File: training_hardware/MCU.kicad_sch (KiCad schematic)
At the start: 2 parts, among them J1 RJ45_LED_Shielded, U1 Teensy4.1_DEV-16771

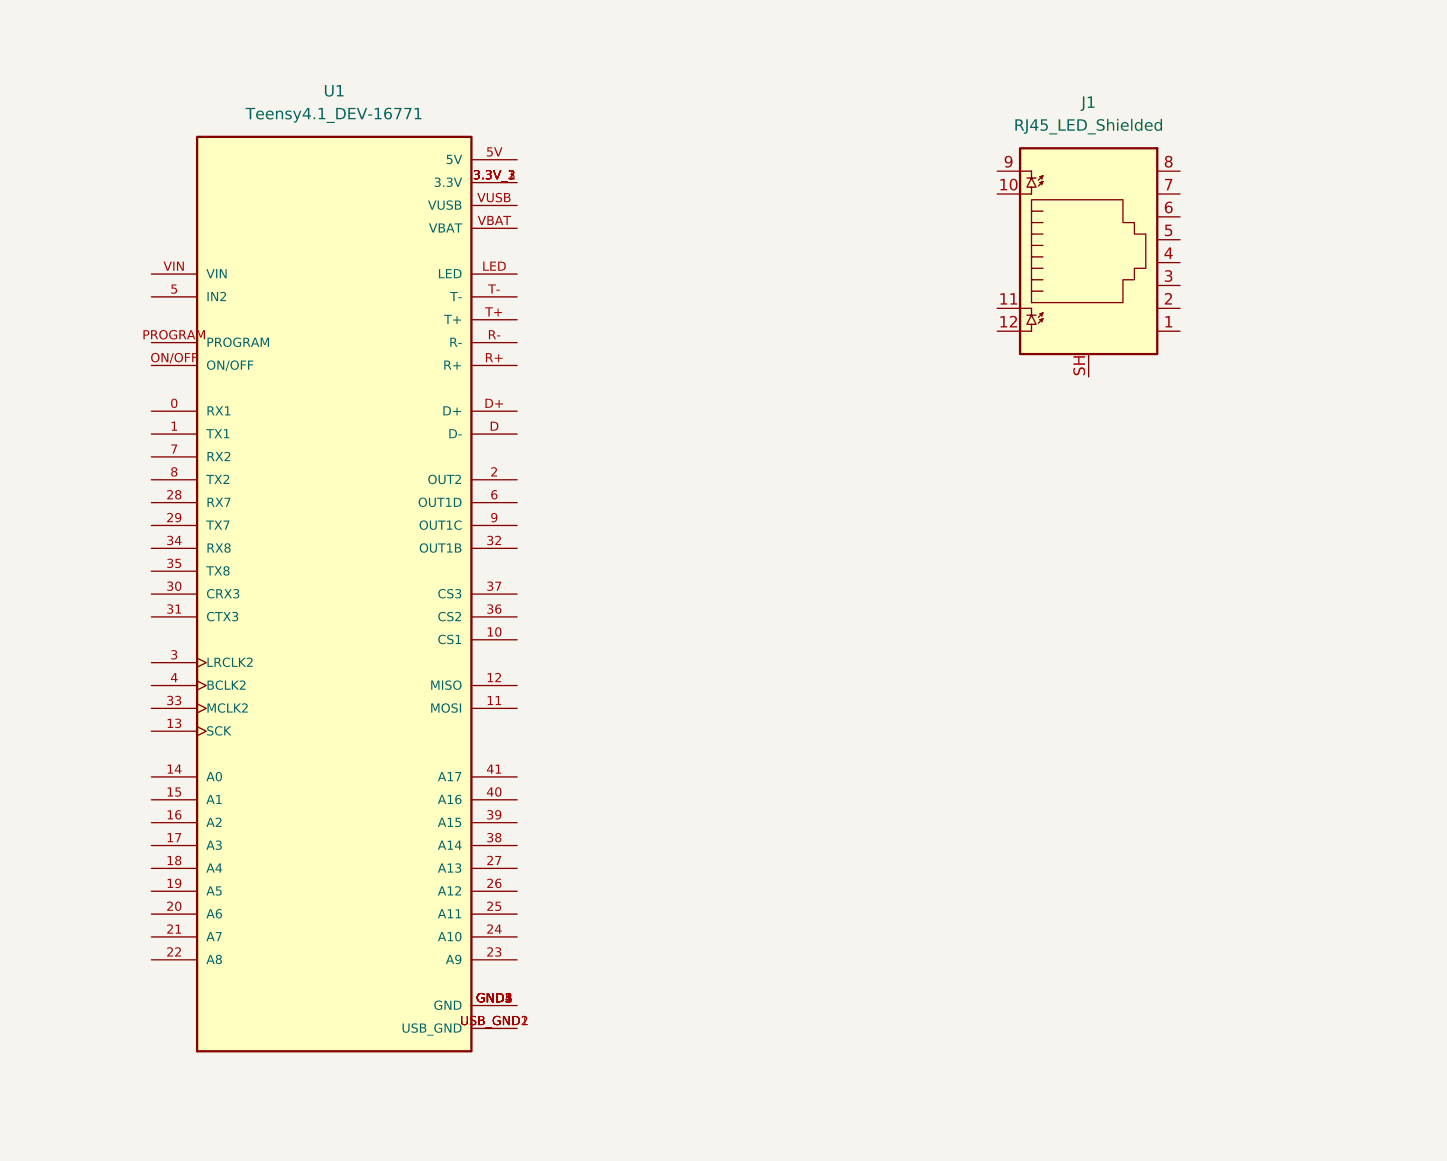
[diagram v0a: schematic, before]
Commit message: add ethernet
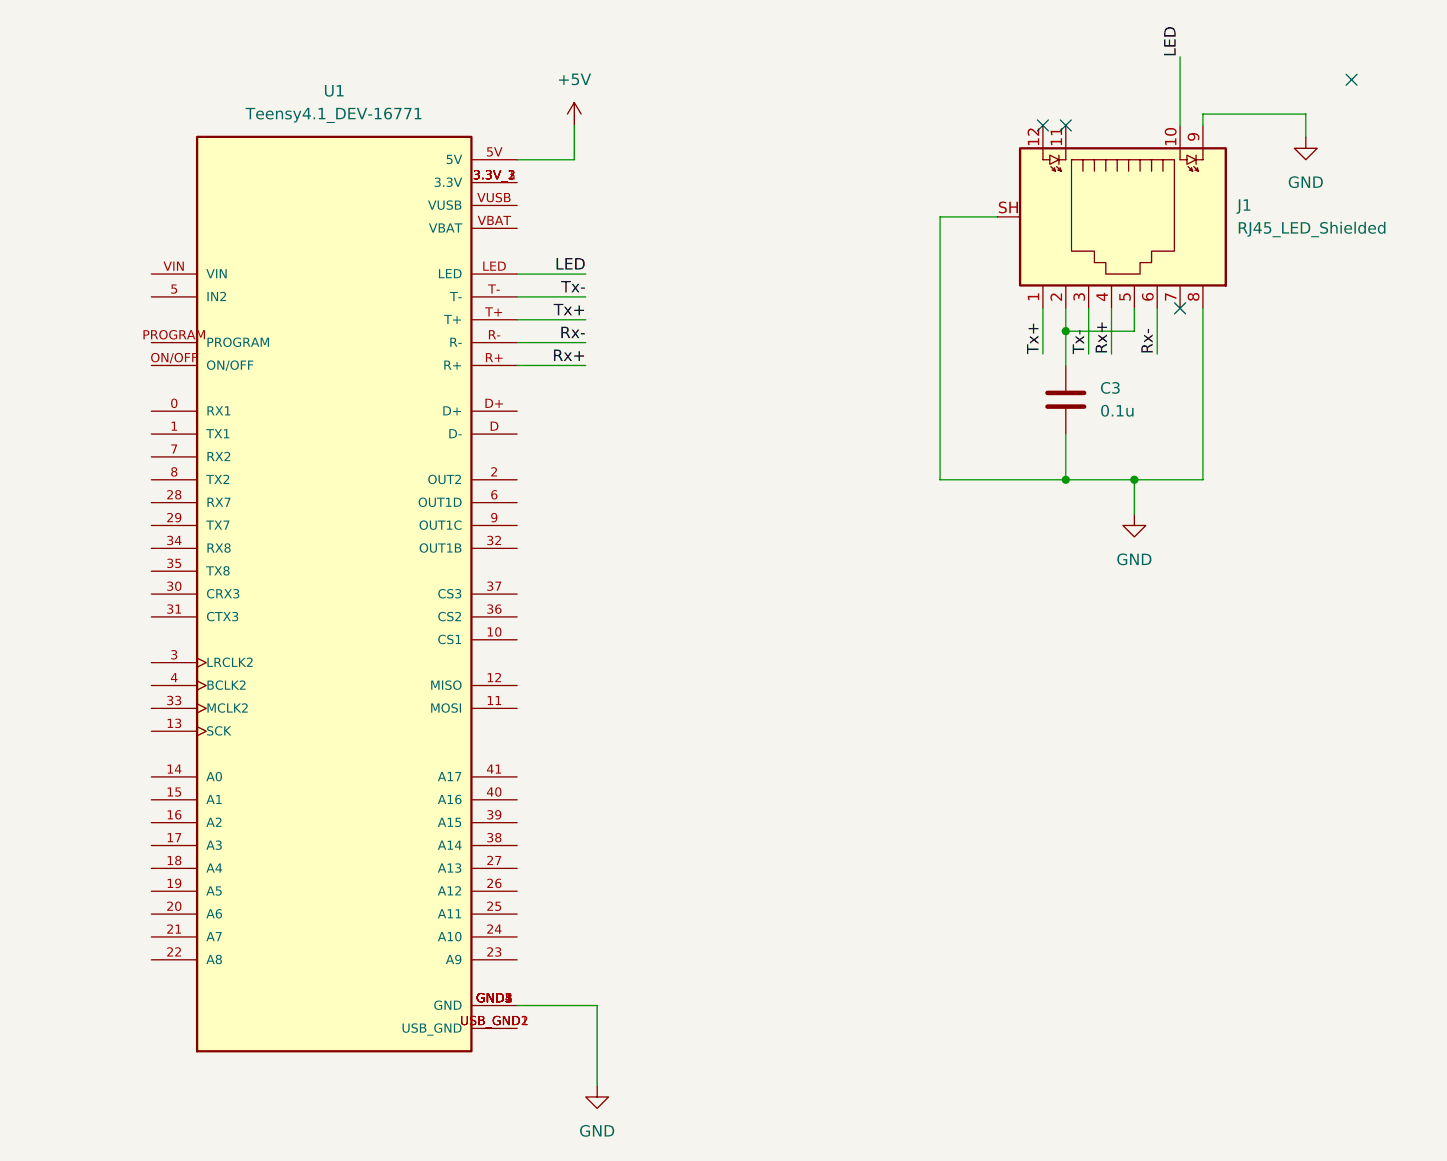
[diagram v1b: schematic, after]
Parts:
- added C3: 0.1u, symbol Device:C
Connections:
- net +5V: now reaches U1.5V
- net GND: now reaches U1.GND1 (GND), U1.GND2 (GND), U1.GND3 (GND), U1.GND4 (GND), U1.GND5 (GND)
- net GND: now also J1.8, J1.9, J1.SH, C3.2
- net LED: now reaches U1.LED
- net LED: now also J1.10
- net Rx+: now reaches U1.R+
- net Rx+: now also J1.4
- net Rx-: now reaches U1.R-
- net Rx-: now also J1.6
- net Tx+: now reaches U1.T+
- net Tx+: now also J1.1
- net Tx-: now reaches U1.T-
- net Tx-: now also J1.3
- net at J1.2: now also J1.5, C3.1
- no-connect marks 0 -> 4
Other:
- moved on the sheet: J1

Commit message: finish schematic
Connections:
- net STBY: now reaches U1.2 (OUT2)
- net CTX1: now reaches U1.22 (A8)
- net CRX1: now reaches U1.23 (A9)
- net +3V3: now reaches U1.3.3V_1 (3.3V), U1.3.3V_2 (3.3V), U1.3.3V_3 (3.3V)
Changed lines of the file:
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@@
+	(wire
+		(pts
+			(xy 121.92 140.97) (xy 128.27 140.97)
+		)
+		(stroke
+			(width 0)
+			(type default)
+		)
+	)
 	(wire
 		(pts
@@
 	(wire
 		(pts
+			(xy 73.66 140.97) (xy 81.28 140.97)
+		)
+		(stroke
+			(width 0)
+			(type default)
+		)
+	)
+	(wire
+		(pts
 			(xy 168.91 58.42) (xy 168.91 87.63)
 		)
@@
 	(wire
 		(pts
+			(xy 133.35 48.26) (xy 133.35 54.61)
+		)
+		(stroke
+			(width 0)
+			(type default)
+		)
+	)
+	(wire
+		(pts
 			(xy 190.5 87.63) (xy 190.5 91.44)
 		)
@@
 	(wire
 		(pts
+			(xy 133.35 54.61) (xy 121.92 54.61)
+		)
+		(stroke
+			(width 0)
+			(type default)
+		)
+	)
+	(wire
+		(pts
 			(xy 190.5 68.58) (xy 190.5 71.12)
 		)
@@
 		(pts
 			(xy 187.96 68.58) (xy 187.96 73.66)
+		)
+		(stroke
+			(width 0)
+			(type default)
+		)
+	)
+	(wire
+		(pts
+			(xy 121.92 87.63) (xy 132.08 87.63)
 		)
 		(stroke
@@
 			)
 			(justify left bottom)
+		)
+	)
+	(hierarchical_label "CRX1"
+		(shape input)
+		(at 128.27 140.97 0)
+		(effects
+			(font
+				(size 1.27 1.27)
+			)
+			(justify left)
+		)
+	)
+	(hierarchical_label "STBY"
+		(shape output)
+		(at 132.08 87.63 0)
+		(effects
+			(font
+				(size 1.27 1.27)
+			)
+			(justify left)
+		)
+	)
+	(hierarchical_label "CTX1"
+		(shape output)
+		(at 73.66 140.97 180)
+		(effects
+			(font
+				(size 1.27 1.27)
+			)
+			(justify right)
 		)
 	)
@@
 					(unit 1)
 				)
+			)
+		)
+	)
+	(symbol
+		(lib_id "power:+3V3")
+		(at 133.35 48.26 0)
+		(unit 1)
+		(exclude_from_sim no)
+		(in_bom yes)
+		(on_board yes)
+		(dnp no)
+		(fields_autoplaced yes)
+		(property "Reference" "#PWR016"
+			(at 133.35 52.07 0)
+			(effects
+				(font
+					(size 1.27 1.27)
+				)
+				(hide yes)
+			)
+		)
+		(property "Value" "+3V3"
+			(at 133.35 43.18 0)
+			(effects
+				(font
+					(size 1.27 1.27)
+				)
+			)
+		)
+		(property "Footprint" ""
+			(at 133.35 48.26 0)
+			(effects
+				(font
+					(size 1.27 1.27)
+				)
+				(hide yes)
+			)
+		)
+		(property "Datasheet" ""
+			(at 133.35 48.26 0)
+			(effects
+				(font
+					(size 1.27 1.27)
+				)
+				(hide yes)
+			)
+		)
+		(property "Description" "Power symbol creates a global label with name \"+3V3\""
+			(at 133.35 48.26 0)
+			(effects
+				(font
+					(size 1.27 1.27)
+				)
+				(hide yes)
+			)
+		)
+		(pin "1"
+		)
+		(instances
+			(project ""
+				(path "/ce6aff0a-6a24-4161-b195-5f43ae1bbb8d/d6ba2c96-7798-41d7-8545-f411ee5f18eb"
+					(reference "#PWR016")
+					(unit 1)
+				)
